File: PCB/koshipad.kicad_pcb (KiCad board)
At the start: 2 copper layers, 96 x 92.8 mm, 35 parts, among them J2 Conn_01x04_Pin, SW1 SW_Push_45deg, SW10 RotaryEncoder_Switch, SW2 SW_Push_45deg, SW3 SW_Push_45deg, SW4 SW_Push_45deg, SW5 SW_Push_45deg, SW6 SW_Push_45deg, SW7 SW_Push_45deg, SW8 SW_Push_45deg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

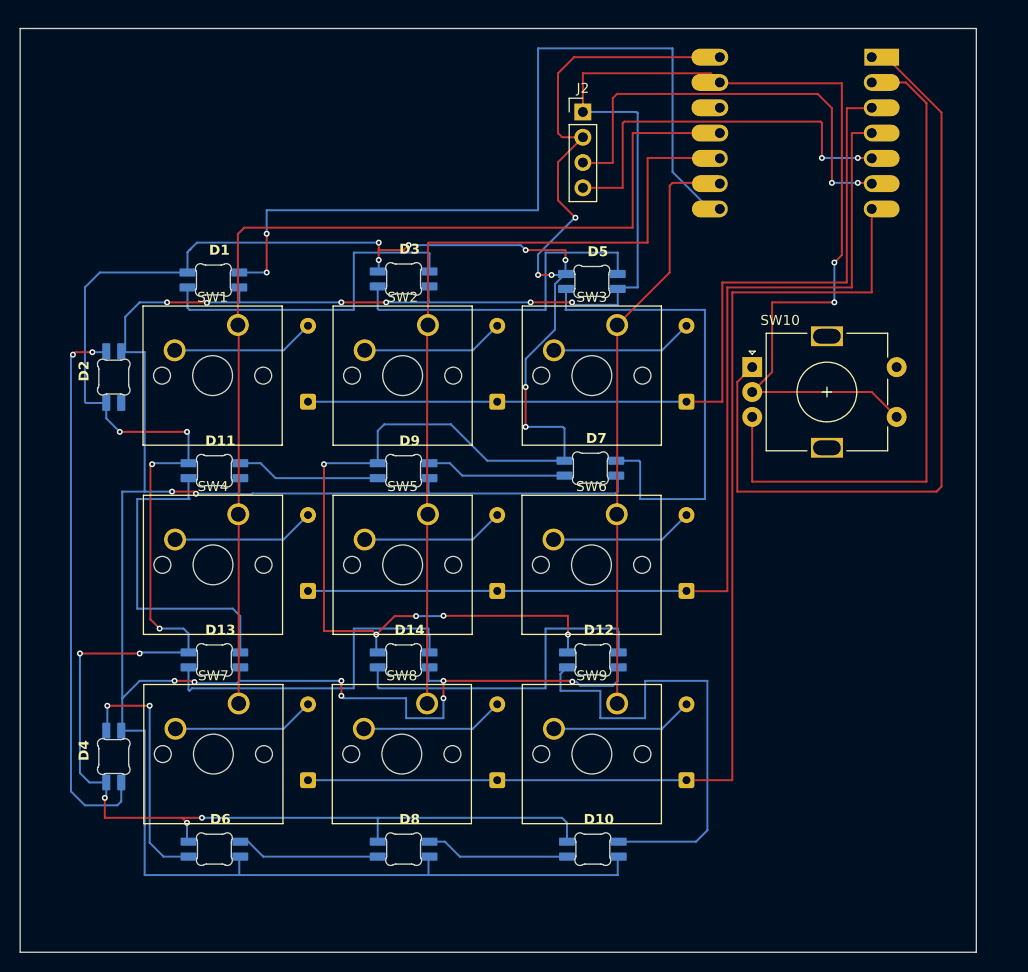
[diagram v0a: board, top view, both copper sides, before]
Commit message: added bocchi sticker in PCB
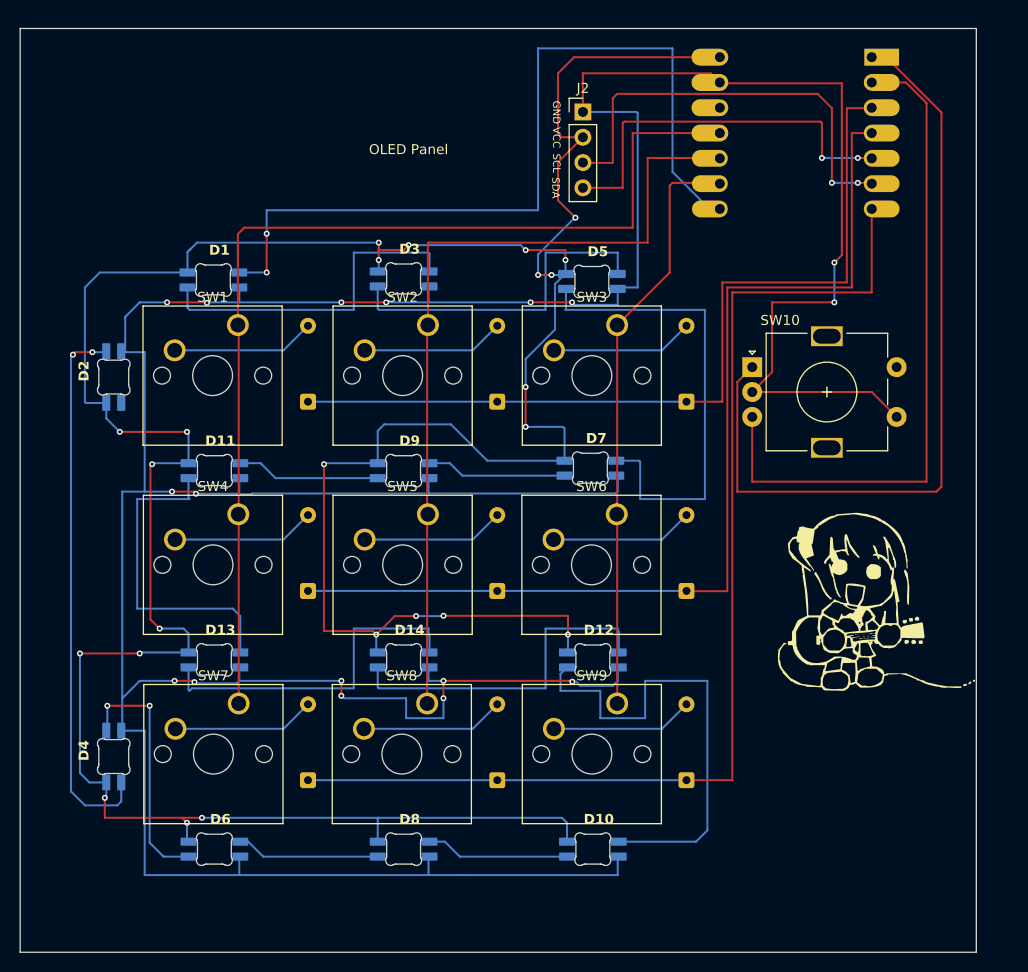
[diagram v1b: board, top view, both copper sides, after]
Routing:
- net (no net): track 0.57 -> 0.00 mm
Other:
- board text added: "GND"
- board text added: "OLED Panel"
- board text added: "SCL"
- board text added: "SDA"
- board text added: "VCC"

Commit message: made changes in pcb
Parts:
- added REF**: MountingHole_3.2mm_M3, MountingHole:MountingHole_3.2mm_M3, F.Cu at (84.1, 129.7)
- added REF**: MountingHole_3.2mm_M3, MountingHole:MountingHole_3.2mm_M3, F.Cu at (173.6, 45.3)
- added REF**: MountingHole_3.2mm_M3, MountingHole:MountingHole_3.2mm_M3, F.Cu at (83.8, 45.3)
- added REF**: MountingHole_3.2mm_M3, MountingHole:MountingHole_3.2mm_M3, F.Cu at (173.8, 129.7)
- moved U2 0.86 mm to (156.0, 51.4)
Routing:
- net GND: track 397.5 -> 391.9 mm
- net ENC_A: track 80.7 -> 82.4 mm
- net Row 2: track 114.0 -> 112.7 mm
- net column 1: track 84.1 -> 82.8 mm
- net column 0: track 105.3 -> 104.2 mm
- net column 2: track 59.4 -> 58.3 mm
- net Row 1: track 102.6 -> 101.7 mm
- net +5V: track 340.4 -> 339.6 mm
- net SDA: track 39.1 -> 38.5 mm
- net Row 0: track 86.1 -> 85.6 mm
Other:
- board size 96 x 92.8 mm -> 99.2 x 92.8 mm
